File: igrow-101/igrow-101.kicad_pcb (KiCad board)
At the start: 2 copper layers, 49.8 x 39.5 mm, 34 parts, among them P1 CONN_02X05, P2 CONN_01X01, P3 CONN_01X01, P4 CONN_01X01, P5 CONN_01X01, Q1 NPN, Q2 NPN, Q3 NPN, SW1 SW_PUSH, U1 NRF51822-MODULE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

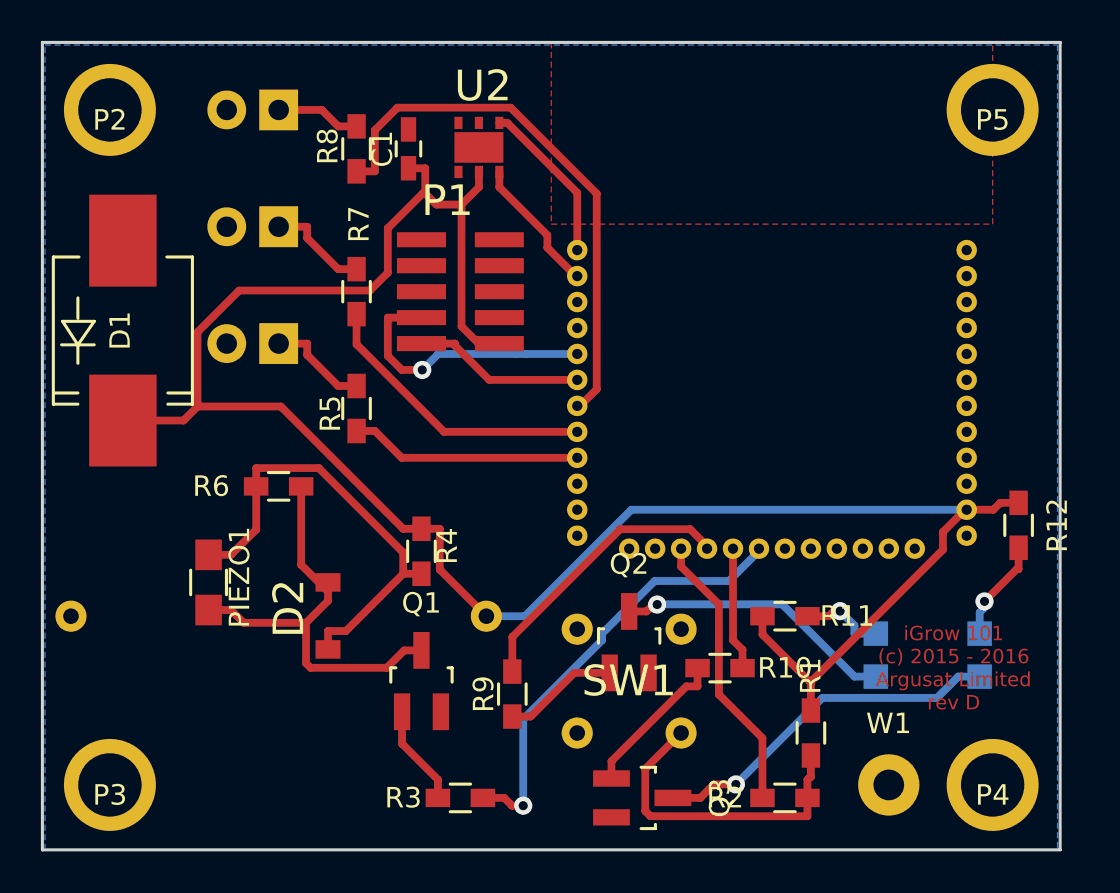
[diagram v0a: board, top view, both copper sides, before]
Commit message: Correct sizing for module, button cell holder through-holes and enlarge SHT21 pads to allow hand soldering if required.
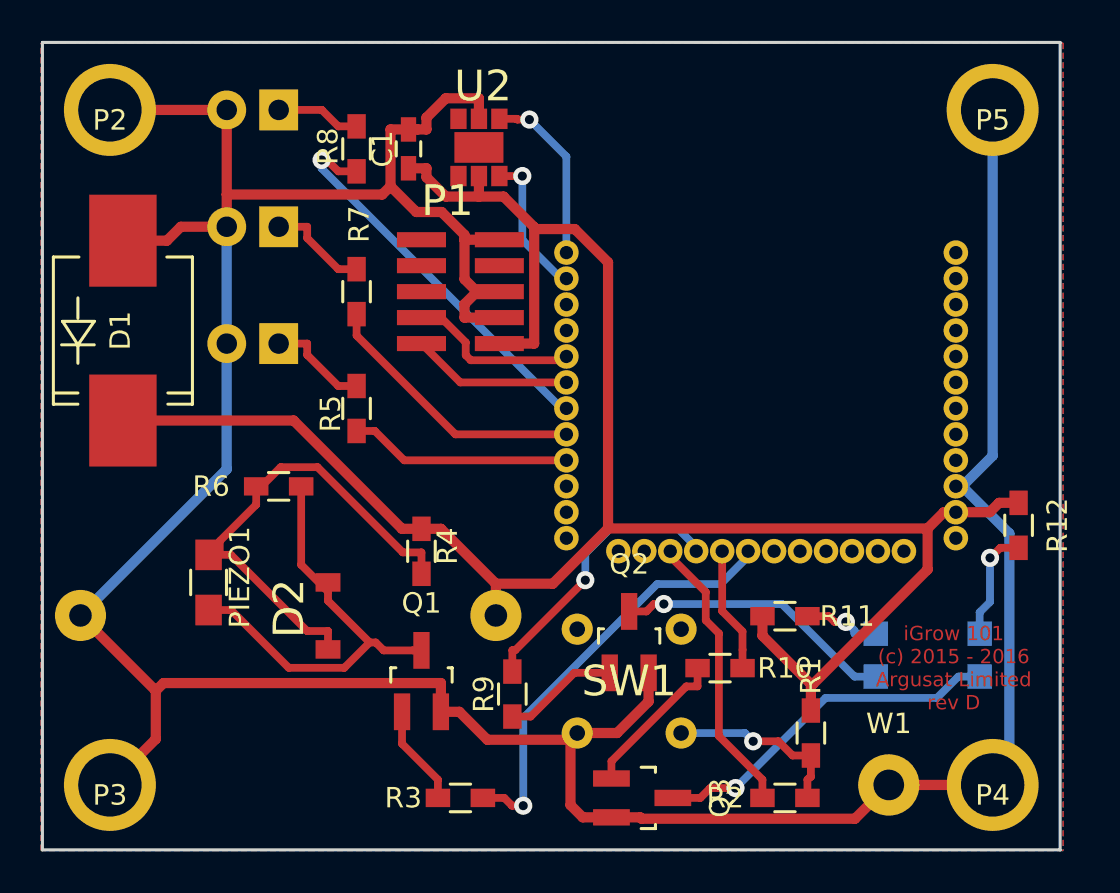
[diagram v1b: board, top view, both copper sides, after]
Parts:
- C1: value C -> 100nF
- R1, R10, R9: value R -> 10kR
- R11, R12: value R -> 620R
- R2: value R -> 150R
- R5, R7, R8: value R -> 220R
- U2: footprint igrow:SHT21 -> igrow:SHT21_HandSoldering
- moved U1 0.54 mm to (176.0, 103.5)
- moved BT1 0.47 mm to (153.5, 121.2)
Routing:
- net GND: track 0.00 -> 168.9 mm
- net Net-(R8-Pad1): track 26.8 -> 19.2 mm, vias 0 -> 1
- net Net-(R1-Pad2): track 15.6 -> 8.97 mm, vias 0 -> 1
- net Net-(P1-Pad4): track 13.4 -> 8.40 mm, vias 1 -> 0
- net VCC: track 102.1 -> 99.3 mm
- net Net-(D2-Pad2): track 22.4 -> 23.7 mm
- net Net-(R7-Pad1): track 14.0 -> 13.3 mm
- net Net-(U1-Pad36): track 8.03 -> 8.74 mm, vias 0 -> 1
- net Net-(R3-Pad2): track 21.6 -> 21.0 mm
- net Net-(P1-Pad2): track 8.42 -> 7.88 mm
- net Net-(D2-Pad1): track 21.2 -> 21.7 mm
- net Net-(U1-Pad35): track 6.71 -> 7.18 mm, vias 0 -> 1
- net Net-(R9-Pad2): track 13.9 -> 13.8 mm, vias 0 -> 1
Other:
- net class GND added: clearance 0.254, trace_width 0.5, via_dia 1.1, via_drill 0.95
- net class VCC added: clearance 0.254, trace_width 0.5, via_dia 1.1, via_drill 0.95

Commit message: Hardware revision F
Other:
- board text added: "iGrow 101 (c) 2016 Argusat Limited"
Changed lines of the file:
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@@
     (links 57)
     (no_connects 0)
-    (area 131.242999 93.142999 181.177001 132.790001)
+    (area 129.146 91.554 182.887334 133.669)
     (thickness 1.6)
-    (drawings 9)
+    (drawings 10)
     (tracks 245)
     (zones 0)
@@
     (tags "capacitor 0603")
     (attr smd)
-    (fp_text reference C1 (at 0 -1.27 90) (layer F.SilkS)
+    (fp_text reference C1 (at 2.675 -0.475 180) (layer F.SilkS)
       (effects (font (size 1 1) (thickness 0.15)))
     )
@@
     (tags "resistor 0603")
     (attr smd)
-    (fp_text reference R1 (at -2.794 0 270) (layer F.SilkS)
+    (fp_text reference R1 (at 0 1.66 270) (layer F.SilkS)
       (effects (font (size 1 1) (thickness 0.15)))
     )
@@
     (tags "resistor 0603")
     (attr smd)
-    (fp_text reference R2 (at -2.921 0) (layer F.SilkS)
+    (fp_text reference R2 (at 0.11 1.575) (layer F.SilkS)
       (effects (font (size 1 1) (thickness 0.15)))
     )
@@
     (tags "resistor 0603")
     (attr smd)
-    (fp_text reference R3 (at -2.794 0) (layer F.SilkS)
+    (fp_text reference R3 (at -0.015 1.575) (layer F.SilkS)
       (effects (font (size 1 1) (thickness 0.15)))
     )
@@
     (tags "resistor 0603")
     (attr smd)
-    (fp_text reference R4 (at -0.254 -1.27 270) (layer F.SilkS)
+    (fp_text reference R4 (at -0.11 -1.89 270) (layer F.SilkS)
       (effects (font (size 1 1) (thickness 0.15)))
     )
@@
     (tags "resistor 0603")
     (attr smd)
-    (fp_text reference R5 (at -0.254 -1.27 90) (layer F.SilkS)
+    (fp_text reference R5 (at 0.125 1.815 90) (layer F.SilkS)
       (effects (font (size 1 1) (thickness 0.15)))
     )
@@
     (tags "resistor 0603")
     (attr smd)
-    (fp_text reference R6 (at -3.302 0) (layer F.SilkS)
+    (fp_text reference R6 (at -0.125 -1.685) (layer F.SilkS)
       (effects (font (size 1 1) (thickness 0.15)))
     )
@@
     (tags "resistor 0603")
     (attr smd)
-    (fp_text reference R8 (at 0.127 -1.397 90) (layer F.SilkS)
+    (fp_text reference R8 (at 2.675 -0.435 180) (layer F.SilkS)
       (effects (font (size 1 1) (thickness 0.15)))
     )
@@
     (tags "resistor 0603")
     (attr smd)
-    (fp_text reference R10 (at 3.175 0) (layer F.SilkS)
+    (fp_text reference R10 (at 0.035 1.425) (layer F.SilkS)
       (effects (font (size 1 1) (thickness 0.15)))
     )
@@
     (tags "resistor 0603")
     (attr smd)
-    (fp_text reference R11 (at 3.048 0) (layer F.SilkS)
+    (fp_text reference R11 (at 0.11 1.465) (layer F.SilkS)
       (effects (font (size 1 1) (thickness 0.15)))
     )
@@
   (module igrow:SPSTSW (layer F.Cu)
     (at 162.56 127 180)
-    (fp_text reference SW1 (at 2.54 2.54 180) (layer F.SilkS)
+    (fp_text reference SW1 (at 5.31 6.75 360) (layer F.SilkS)
       (effects (font (size 1.5 1.5) (thickness 0.15)))
     )
@@
     (tags "resistor 0805")
     (attr smd)
-    (fp_text reference PIEZO1 (at -0.254 -1.524 270) (layer F.SilkS)
+    (fp_text reference PIEZO1 (at 0.116 -2.054 270) (layer F.SilkS)
       (effects (font (size 1 1) (thickness 0.15)))
     )
@@
   (module igrow:harwin_m50-3600542 (layer F.Cu)
     (at 153.67 107.95 180)
-    (fp_text reference P1 (at 2.54 6.985 180) (layer F.SilkS)
+    (fp_text reference P1 (at 1.67 -2.05 180) (layer F.SilkS)
       (effects (font (size 1.5 1.5) (thickness 0.15)))
     )
@@
     (descr "LED 5mm round vertical")
     (tags "LED 5mm round vertical")
-    (fp_text reference D3 (at 1.524 -4.064 180) (layer B.SilkS)
+    (fp_text reference D3 (at -1.875 2.45 180) (layer B.SilkS)
       (effects (font (size 1 1) (thickness 0.15)) (justify mirror))
     )
@@
     (descr "LED 5mm round vertical")
     (tags "LED 5mm round vertical")
-    (fp_text reference D4 (at 1.524 -4.064 180) (layer B.SilkS)
+    (fp_text reference D4 (at 4.875 2.485 180) (layer B.SilkS)
       (effects (font (size 1 1) (thickness 0.15)) (justify mirror))
     )
@@
     (descr "LED 5mm round vertical")
     (tags "LED 5mm round vertical")
-    (fp_text reference D5 (at 1.524 -4.064 180) (layer B.SilkS)
+    (fp_text reference D5 (at 4.875 2.27 180) (layer B.SilkS)
       (effects (font (size 1 1) (thickness 0.15)) (justify mirror))
     )
@@
     (tags "resistor 0603")
     (attr smd)
-    (fp_text reference R12 (at 0 -1.9 270) (layer F.SilkS)
+    (fp_text reference R12 (at -2.84 -0.18 360) (layer F.SilkS)
       (effects (font (size 1 1) (thickness 0.15)))
     )
@@
   (module igrow:MountingHole_M3 (layer F.Cu)
     (at 134.62 96.52)
-    (fp_text reference P2 (at 0 0.5) (layer F.SilkS)
+    (fp_text reference P2 (at -2.12 2.73) (layer F.SilkS)
       (effects (font (size 1 1) (thickness 0.15)))
     )
@@
   (module igrow:MountingHole_M3 (layer F.Cu)
     (at 134.62 129.54)
-    (fp_text reference P3 (at 0 0.5) (layer F.SilkS)
+    (fp_text reference P3 (at -1.87 -2.79) (layer F.SilkS)
       (effects (font (size 1 1) (thickness 0.15)))
     )
@@
   (module igrow:MountingHole_M3 (layer F.Cu)
     (at 177.8 129.54)
-    (fp_text reference P4 (at 0 0.5) (layer F.SilkS)
+    (fp_text reference P4 (at -2.3 -2.54) (layer F.SilkS)
       (effects (font (size 1 1) (thickness 0.15)))
     )
@@
   (module igrow:MountingHole_M3 (layer F.Cu)
     (at 177.8 96.52)
-    (fp_text reference P5 (at 0 0.5) (layer F.SilkS)
+    (fp_text reference P5 (at 1.45 3.23) (layer F.SilkS)
       (effects (font (size 1 1) (thickness 0.15)))
     )
@@
     (tags SOT-23)
     (attr smd)
-    (fp_text reference Q1 (at 0 -3.81) (layer F.SilkS)
+    (fp_text reference Q1 (at 0.14 3.54) (layer F.SilkS)
       (effects (font (size 1 1) (thickness 0.15)))
     )
@@
     (tags SOT-23)
     (attr smd)
-    (fp_text reference Q2 (at 0 -3.81) (layer F.SilkS)
+    (fp_text reference Q2 (at -0.02 3.445) (layer F.SilkS)
       (effects (font (size 1 1) (thickness 0.15)))
     )
@@
     (tags SOT-23)
     (attr smd)
-    (fp_text reference Q3 (at 0 -3.81 270) (layer F.SilkS)
+    (fp_text reference Q3 (at -2.425 0.905 540) (layer F.SilkS)
       (effects (font (size 1 1) (thickness 0.15)))
     )
@@
     (tags "Mesurement Point Round Trough Hole 3mm 1.5mm")
     (attr virtual)
-    (fp_text reference W1 (at 0 -3) (layer F.SilkS)
+    (fp_text reference W1 (at -1.22 -2.29) (layer F.SilkS)
       (effects (font (size 1 1) (thickness 0.15)))
     )
@@
       (net 1 GND))
   )
+  (gr_text "iGrow 101\n(c) 2016\nArgusat Limited" (at 150 101.25) (layer B.SilkS)
+    (effects (font (size 0.75 0.75) (thickness 0.1875)) (justify mirror))
+  )
   (target plus (at 134.62 129.54) (size 5) (width 0.15) (layer Edge.Cuts))
